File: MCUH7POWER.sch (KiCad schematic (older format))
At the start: 54 parts, among them J2 S1G20_01x01K, J3 S1G20_01x02, J4 USB_C_Receptacle_flat, U3 STM32H757XIH6, U5 NCP1117-3.3, U7 PESD2ETH-X

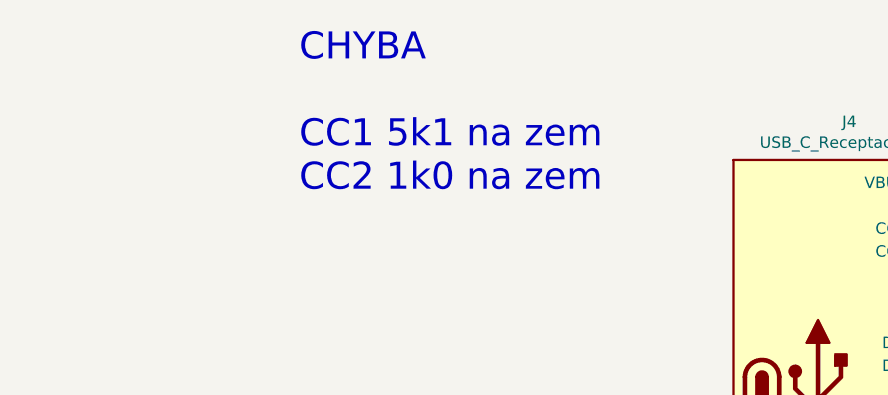
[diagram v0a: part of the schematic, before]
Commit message: MCUH7POWER bug description added
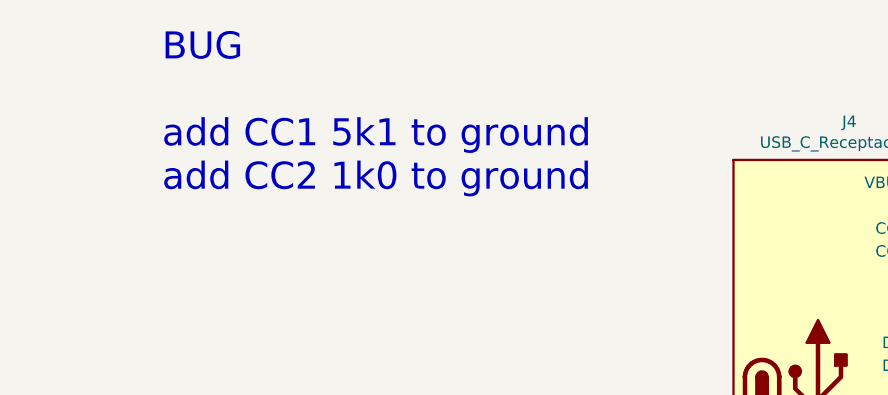
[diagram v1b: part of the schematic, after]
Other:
- note added: "BUG\n\nadd CC1 5k1 to ground\nadd CC2 1k0 to ground"
- note removed: "CHYBA\n\nCC1 5k1 na zem\nCC2 1k0 na zem"
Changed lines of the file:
@@
 	1    0    0    -1
 $EndComp
-Wire Wire Line
-	13350 1450 13650 1450
 Text Label 15250 1450 2    50   ~ 0
 VBUS
@@
 Wire Wire Line
 	13350 1650 13450 1650
-Wire Wire Line
-	13650 1650 13650 1450
-Connection ~ 13650 1450
 $Comp
 L power:GND #PWR0130
@@
 	1    0    0    -1
 $EndComp
-Wire Wire Line
-	13650 1450 13900 1450
 Connection ~ 13900 1450
 Wire Wire Line
@@
 	1    0    0    -1
 $EndComp
-Text Notes 10450 1500 0    118  ~ 0
-CHYBA\n\nCC1 5k1 na zem\nCC2 1k0 na zem
+Text Notes 9850 1500 0    118  ~ 0
+BUG\n\nadd CC1 5k1 to ground\nadd CC2 1k0 to ground
+Wire Wire Line
+	13650 1450 13900 1450
+Wire Wire Line
+	13350 1450 13650 1450
+Connection ~ 13650 1450
+Wire Wire Line
+	13650 1650 13650 1450
 $EndSCHEMATC
